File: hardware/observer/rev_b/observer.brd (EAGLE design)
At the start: 49 x 59.9 mm, 55 parts, among them J1 CON_HEADER_2X05-SMD+SHROUDED, J2 CON_HEADER_2X05-SMD+SHROUDED, J3 TC2030-CC2538-BL-NL, J4 JUMPER-PTH-2-NO, J5 PINHD-2X8/SMD, J6 CON_HEADER_2X05-PTH+SHROUDED_A, P9/P8 BBB_HEADER, U1 LPS331AP, U2 MPU-9250, U3 SI1147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

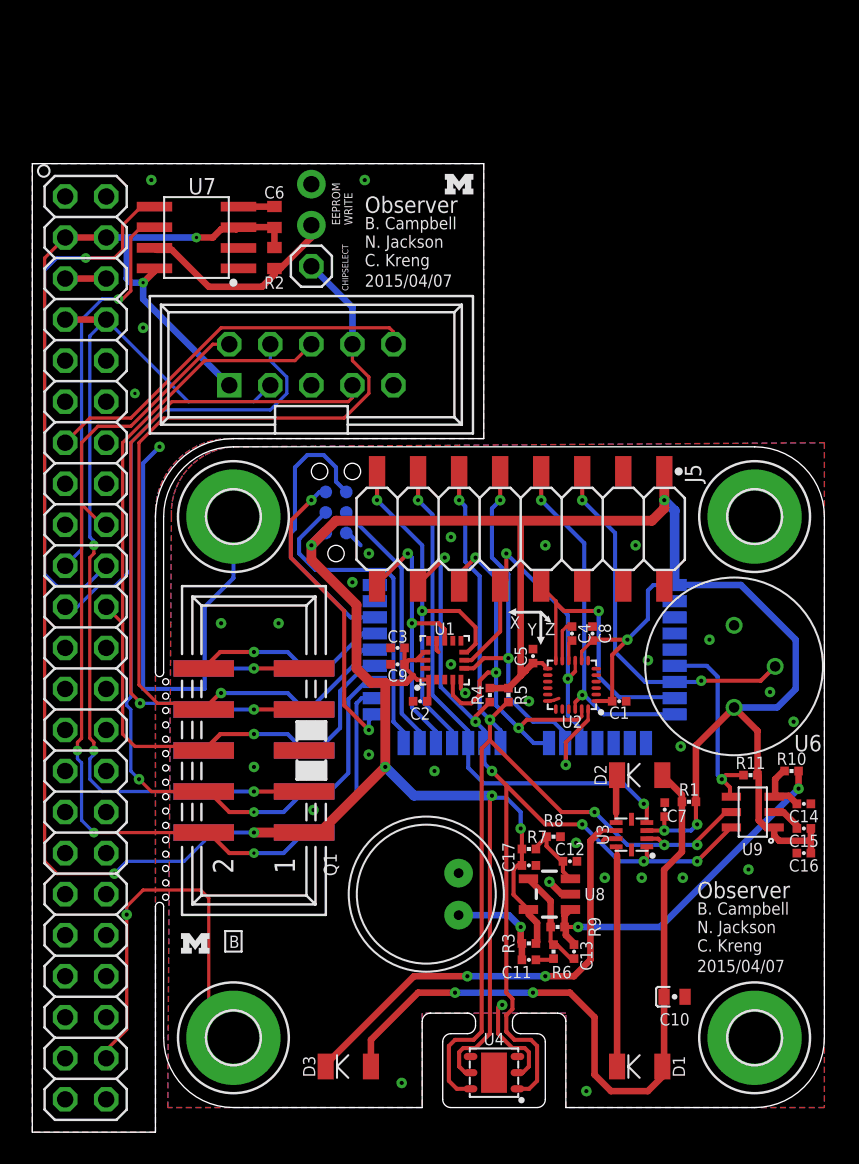
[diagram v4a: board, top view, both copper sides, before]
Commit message: Renamed passives in order of increasing value, highlighted parts needed in bom
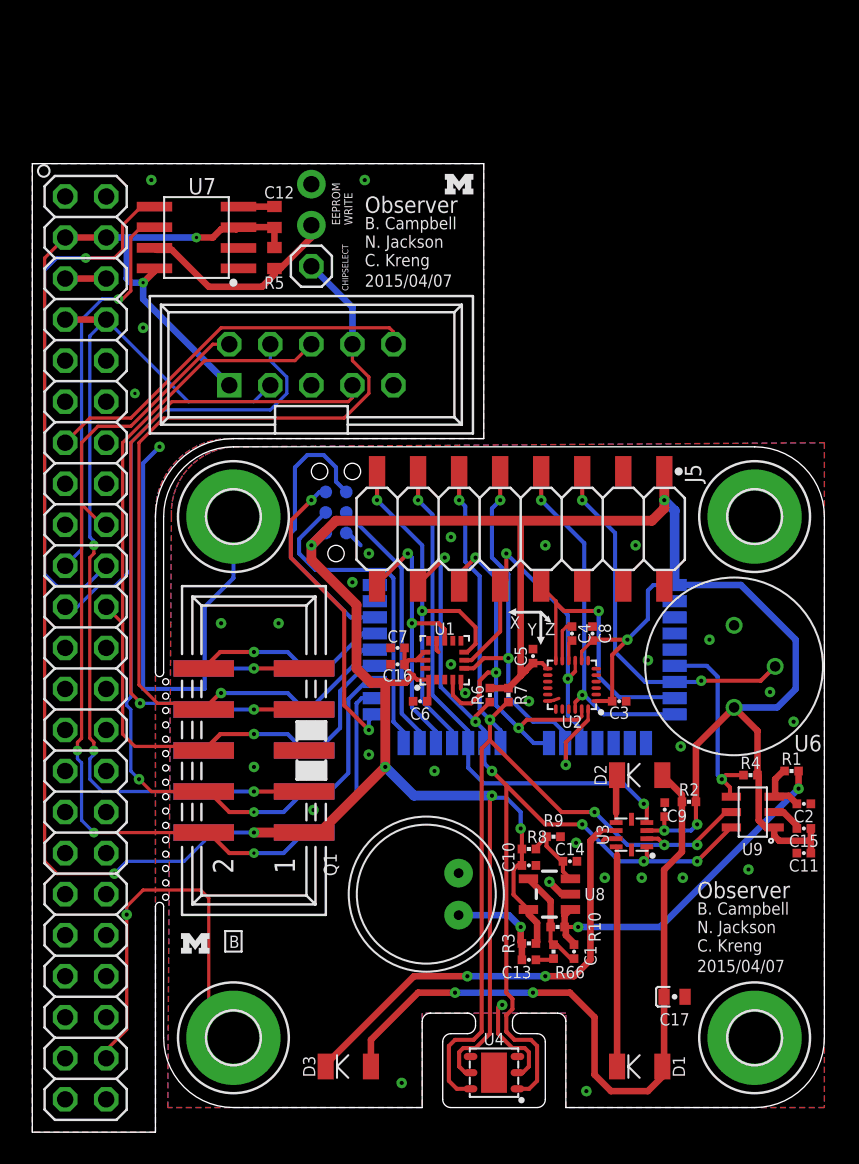
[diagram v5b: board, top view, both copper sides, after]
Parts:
- removed R11: 5k, passives:0402_RES
- added R66: 10k, passives:0402_RES
- C1: value 10nF -> 12pF
- C10: value 22uF -> 0.1uF; device passives:CAP0603 -> passives:0402_CAP
- C11: value 4.7uF -> 0.1uF
- C12: value 4.7uF -> 0.1uF; device passives:0402_CAP -> rcl:C0402
- C13: value 12pF -> 4.7uF
- C14: value 470pF -> 4.7uF
- C16: value 0.1uF -> 10uF
- C17: value 0.1uF -> 22uF; device passives:0402_CAP -> passives:CAP0603
- C2: value 0.1uF -> 470pF
- C3: value 0.1uF -> 10nF
- C6: value 100nF -> 0.1uF; device rcl:C0402 -> passives:0402_CAP
- C9: value 10uF -> 0.1uF
- R1: value 30 -> 22
- R10: value 22 -> 1M
- R2: value 10k 1% -> 30; device rcl:R0402 -> passives:0402_RES
- R4: value 10k -> 5k
- R5: device passives:0402_RES -> rcl:R0402
- R9: value 1M -> 10k
- moved C12 43.9 mm to (15.0, 56.6), turned to 90 degrees
- moved R2 42.3 mm to (40.6, 20.4), turned to 0 degrees
- moved C6 31.3 mm to (24.0, 26.7), turned to 180 degrees
- moved R5 30.7 mm to (15.0, 54.1), turned to 270 degrees
- moved C16 27.7 mm to (22.6, 29.0)
- moved C2 24.6 mm to (47.8, 20.3), turned to 0 degrees
- moved C7 19.3 mm to (22.6, 30.0), turned to 180 degrees
- moved C9 18.8 mm to (39.1, 20.0), turned to 90 degrees
- moved C11 18.3 mm to (47.8, 17.3)
- moved R10 17.4 mm to (32.5, 12.7), turned to 0 degrees
- moved R4 16.9 mm to (44.5, 22.1), turned to 0 degrees
- moved R6 16.4 mm to (28.3, 27.1)
- moved C1 15.7 mm to (33.5, 11.2), turned to 270 degrees
- moved C14 14.9 mm to (33.3, 16.8)
- moved C3 14.1 mm to (36.3, 26.7), turned to 0 degrees
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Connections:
- net GND: now also C10.2, C11.2, C17.NEG, R9.1; no longer C1.2, C10.NEG, C17.2, R8.1
- net MIC_AIN: now also C1.1, R1.1, R10.2; no longer C13.1, R10.1, R9.2
- net MIC_INT: now also R4.1; no longer R11.1
- net N$1: now also C13.2; no longer C11.2
- net N$10: now also C14.1, R8.1, R9.2; no longer C12.1, R7.1, R8.2
- net N$11: now also C2.1, R1.2; no longer C14.1, R10.2
- net N$31: now also R5.2; no longer R2.2
- net N$5: now also C13.1, R66.1; no longer C11.1, R6.1
- net N$8: now also C17.POS, R2.1; no longer C10.POS, R1.1
- net N$9: now also C1.2, R10.1, R66.2; no longer C13.2, R6.2, R9.1
- net SCL: now also R7.1; no longer R5.1
- net SDA: now also R6.1; no longer R4.1
- net VCC: now also C10.1, C11.1, C12.1, R2.2, R5.1, R6.2, R8.2; no longer C1.1, C17.1, C2.1, R1.2, R11.2, R2.1, R5.2

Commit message: Shipped off board, fixed DRU errors.
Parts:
- R4: value 5k -> 4.99k
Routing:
- net GND: track 80.3 -> 32.7 mm
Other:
- board size 49 x 59.9 mm -> 49 x 60.2 mm
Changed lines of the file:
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@@
 <layer number="27" name="tValues" color="7" fill="1" visible="no" active="yes"/>
 <layer number="28" name="bValues" color="7" fill="1" visible="no" active="yes"/>
-<layer number="29" name="tStop" color="7" fill="3" visible="no" active="yes"/>
-<layer number="30" name="bStop" color="7" fill="6" visible="no" active="yes"/>
+<layer number="29" name="tStop" color="7" fill="3" visible="yes" active="yes"/>
+<layer number="30" name="bStop" color="7" fill="6" visible="yes" active="yes"/>
 <layer number="31" name="tCream" color="7" fill="4" visible="no" active="yes"/>
 <layer number="32" name="bCream" color="7" fill="5" visible="no" active="yes"/>
@@
 <rectangle x1="9.271" y1="21.844" x2="11.049" y2="22.86" layer="22" rot="R180"/>
 <rectangle x1="9.271" y1="24.384" x2="11.049" y2="25.4" layer="22" rot="R180"/>
-<wire x1="0" y1="0" x2="0" y2="59.944" width="0" layer="20"/>
+<wire x1="0" y1="0" x2="0" y2="60.198" width="0" layer="20"/>
 <wire x1="0" y1="0" x2="7.62" y2="0" width="0" layer="20"/>
 <wire x1="7.62" y1="0" x2="7.62" y2="13.97" width="0" layer="20"/>
@@
 <wire x1="44.704" y1="1.524" x2="33.02" y2="1.524" width="0" layer="20"/>
 <wire x1="12.446" y1="1.524" x2="24.13" y2="1.524" width="0" layer="20"/>
-<wire x1="27.94" y1="42.926" x2="27.94" y2="59.944" width="0" layer="20"/>
+<wire x1="27.94" y1="42.926" x2="27.94" y2="60.198" width="0" layer="20"/>
 <wire x1="24.13" y1="1.524" x2="24.13" y2="6.858" width="0" layer="20"/>
 <wire x1="12.446" y1="42.926" x2="27.94" y2="42.926" width="0" layer="20"/>
-<wire x1="0" y1="59.944" x2="27.94" y2="59.944" width="0" layer="20"/>
+<wire x1="0" y1="60.198" x2="27.94" y2="60.198" width="0" layer="20"/>
 <text x="19.812" y="56.134" size="0.508" layer="25" font="vector" ratio="12" rot="R90">EEPROM
 WRITE</text>
@@
 </class>
 </classes>
-<designrules name="sunstone-2lyr_v1.0.0.3">
+<designrules name="sunstone-2lyr_v1.0.0.3 *">
 <description language="en">&lt;b&gt;EAGLE Design Rules for *2* Layer Designs (DS)&lt;/b&gt;
 &lt;p&gt;
@@
 <param name="mdViaViaSameLayer" value="8mil"/>
 <param name="mnLayersViaInSmd" value="2"/>
-<param name="mdCopperDimension" value="20mil"/>
+<param name="mdCopperDimension" value="10mil"/>
 <param name="mdDrill" value="16mil"/>
 <param name="mdSmdStop" value="0mil"/>
@@
 <param name="mlMinCreamFrame" value="0mil"/>
 <param name="mlMaxCreamFrame" value="0mil"/>
-<param name="mlViaStopLimit" value="0mil"/>
+<param name="mlViaStopLimit" value="15mil"/>
 <param name="srRoundness" value="0"/>
 <param name="srMinRoundness" value="0mil"/>
@@
 <attribute name="VALUE" x="47.752" y="18.669" size="1.016" layer="27" font="vector" ratio="12" rot="R180" align="bottom-center"/>
 </element>
-<element name="R4" library="passives" package="0402_RES" value="5k" x="44.45" y="22.098" smashed="yes">
+<element name="R4" library="passives" package="0402_RES" value="4.99k" x="44.45" y="22.098" smashed="yes">
 <attribute name="NAME" x="44.45" y="22.479" size="0.762" layer="25" font="vector" ratio="12" align="bottom-center"/>
 <attribute name="VALUE" x="44.45" y="20.701" size="1.016" layer="27" font="vector" ratio="12" align="bottom-center"/>
@@
 <vertex x="7.62" y="0"/>
 <vertex x="0" y="0"/>
-<vertex x="0" y="59.944"/>
-<vertex x="27.94" y="59.944"/>
+<vertex x="0" y="60.452"/>
+<vertex x="27.94" y="60.452"/>
 </polygon>
 <polygon width="0.254" layer="1">
@@
 <vertex x="7.62" y="0"/>
 <vertex x="0" y="0"/>
-<vertex x="0" y="59.944"/>
-<vertex x="27.94" y="59.944"/>
+<vertex x="0" y="60.452"/>
+<vertex x="27.94" y="60.452"/>
 </polygon>
 <wire x1="12.76" y1="57.282" x2="14.976" y2="57.282" width="0.4064" layer="1"/>
@@
 <contactref element="C10" pad="2"/>
 <wire x1="4.572" y1="4.572" x2="4.572" y2="5.08" width="0.2032" layer="1"/>
-<wire x1="4.572" y1="5.08" x2="5.842" y2="6.35" width="0.2032" layer="1"/>
-<wire x1="5.842" y1="6.35" x2="5.842" y2="13.462" width="0.2032" layer="1"/>
-<wire x1="5.842" y1="13.462" x2="5.842" y2="13.97" width="0.2032" layer="1"/>
-<wire x1="5.842" y1="13.97" x2="6.858" y2="14.986" width="0.2032" layer="1"/>
 <wire x1="6.858" y1="14.986" x2="10.414" y2="14.986" width="0.2032" layer="1"/>
-<wire x1="10.414" y1="14.986" x2="10.922" y2="14.478" width="0.2032" layer="1"/>
-<wire x1="10.922" y1="14.478" x2="10.922" y2="7.366" width="0.2032" layer="1"/>
-<wire x1="10.922" y1="7.366" x2="12.446" y2="5.842" width="0.2032" layer="1"/>
 <via x="7.874" y="42.418" extent="1-16" drill="0.254"/>
 <via x="5.842" y="13.462" extent="1-16" drill="0.254"/>
 <via x="44.323" y="16.256" extent="1-16" drill="0.254"/>
-<wire x1="12.446" y1="38.1" x2="12.446" y2="34.29" width="0.254" layer="16"/>
-<wire x1="12.446" y1="34.29" x2="10.668" y2="32.512" width="0.254" layer="16"/>
 <wire x1="10.668" y1="27.432" x2="6.858" y2="27.432" width="0.254" layer="16"/>
-<wire x1="6.858" y1="27.432" x2="6.858" y2="41.402" width="0.254" layer="16"/>
-<wire x1="6.858" y1="41.402" x2="7.874" y2="42.418" width="0.254" layer="16"/>
-<wire x1="10.668" y1="27.432" x2="10.668" y2="32.512" width="0.254" layer="16"/>
 </signal>
 <signal name="N$3">
